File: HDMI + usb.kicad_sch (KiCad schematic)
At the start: 3 parts, among them J2 HDMI_C_1.4, J3 USB_C_Receptacle_USB2.0_16P, J4 USB_C_Receptacle_USB2.0_16P

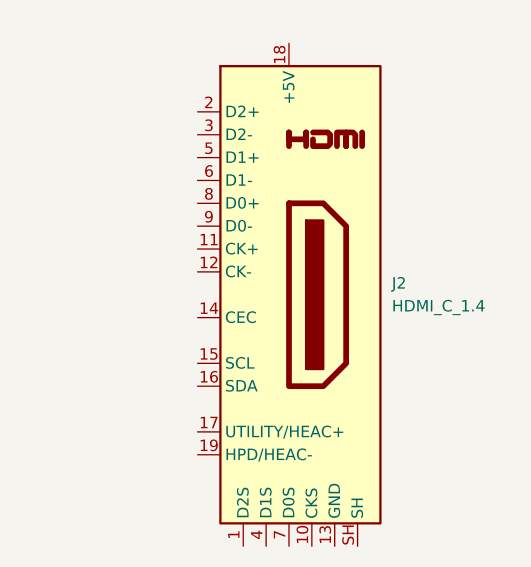
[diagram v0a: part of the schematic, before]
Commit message: расставлены основные блоки и компоненты, подобраны компоненты интерфейса и питания
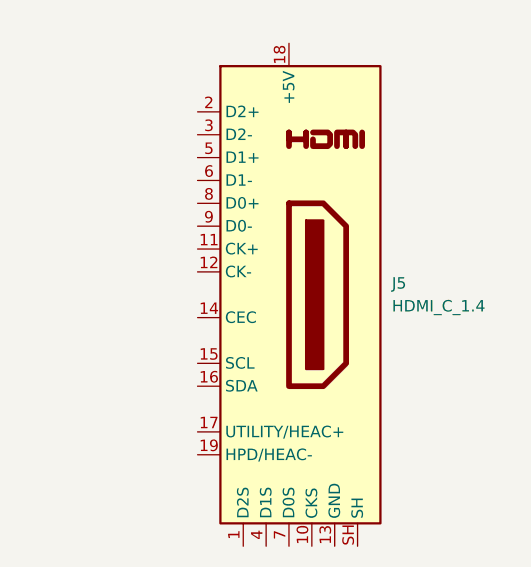
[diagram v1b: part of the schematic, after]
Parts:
- renumbered J2 to J5
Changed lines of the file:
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@@
 		(dnp no)
 		(fields_autoplaced yes)
-		(property "Reference" "J2"
+		(property "Reference" "J5"
 			(at 295.91 147.3199 0)
 			(effects
@@
 			(project ""
 				(path "/b3673bfd-24d8-4789-b63c-c3654dc2bb6e/526c7efe-cb70-49a2-a6ca-c3db3e12ecbe"
-					(reference "J2")
+					(reference "J5")
 					(unit 1)
 				)

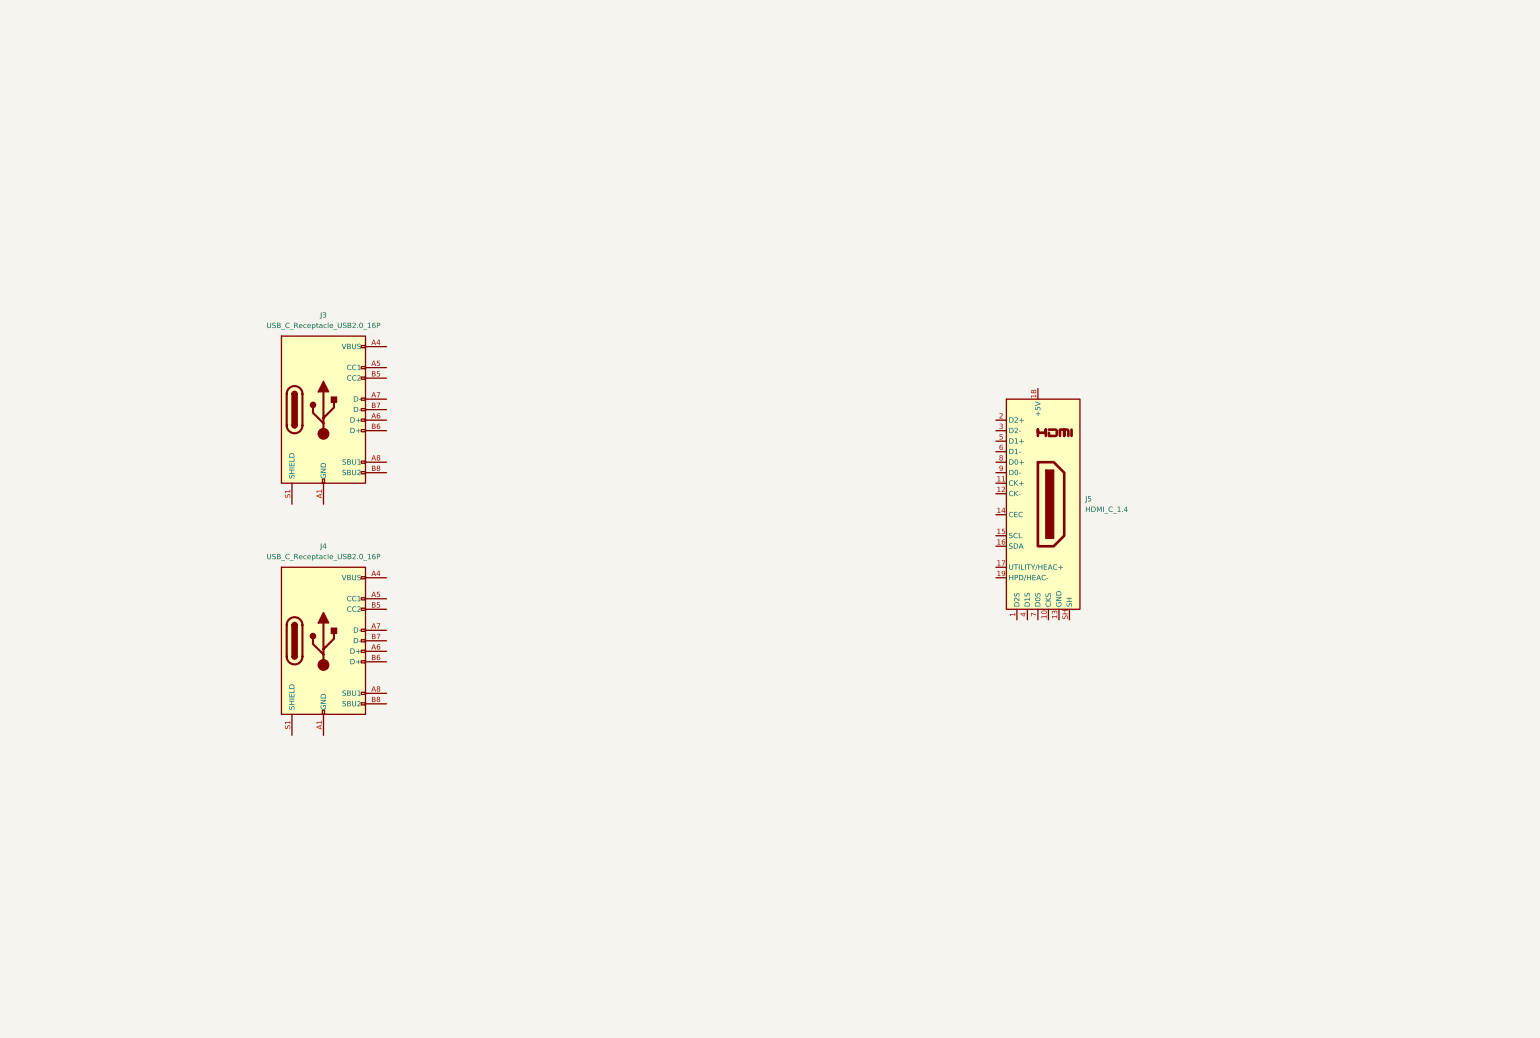
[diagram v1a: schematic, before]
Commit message: Обновлена структура, закончен интерфейс, HDMI Завершено проектирование линий питания и подтяжек для интерфейсов
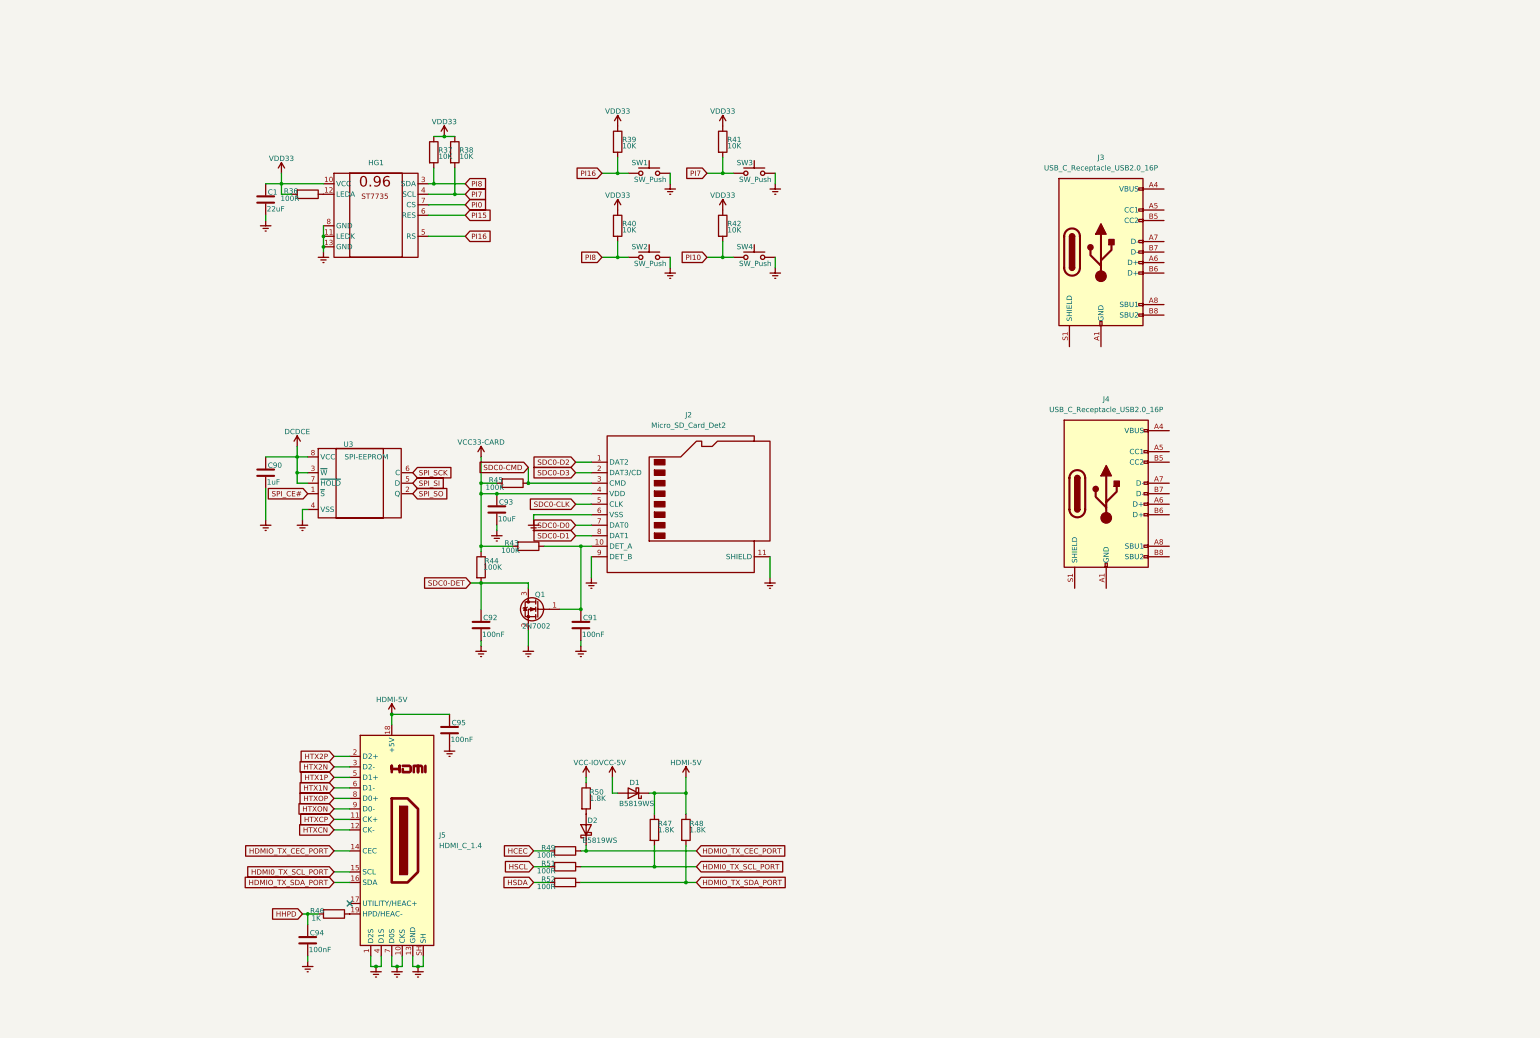
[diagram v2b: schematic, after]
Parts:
- added C1: 22uF, Capacitor_SMD:C_0402_1005Metric, symbol Device:C
- added C90: 1uF, Capacitor_SMD:C_0402_1005Metric, symbol Device:C
- added C91, C92, C94, C95: 100nF, Capacitor_SMD:C_0402_1005Metric, symbol Device:C
- added C93: 10uF, Capacitor_SMD:C_0402_1005Metric, symbol Device:C
- added D1, D2: B5819WS, Diode_SMD:D_SOD-323F, symbol Diode:PMEG4010CEJ
- added HG1: ~, IPS_ST7735_0_96:ST7735 0.96, symbol ST7735 0_96:ST7735_0.96
- added J2: Micro_SD_Card_Det2, Connector_Card:microSD_HC_Hirose_DM3AT-SF-PEJM5, symbol Connector:Micro_SD_Card_Det2
- added Q1: 2N7002, Package_TO_SOT_SMD:SOT-23, symbol Transistor_FET:2N7002
- added R36, R49, R51, R52: 100R, Resistor_SMD:R_0402_1005Metric, symbol Device:R
- added R37, R38, R39, R40, R41, R42: 10K, Resistor_SMD:R_0402_1005Metric, symbol Device:R
- added R43, R44, R45: 100K, Resistor_SMD:R_0402_1005Metric, symbol Device:R
- added R46: 1K, Resistor_SMD:R_0402_1005Metric, symbol Device:R
- added R47, R48, R50: 1.8K, Resistor_SMD:R_0402_1005Metric, symbol Device:R
- added SW1, SW2, SW3, SW4: SW_Push, Button_Switch_SMD:SW_Push_1P1T_NO_Vertical_Wuerth_434133025816, symbol Switch:SW_Push
- added U3: SPI-EEPROM, Package_SO:SOIC-8_3.9x4.9mm_P1.27mm, symbol Memory_EEPROM:M95256-WMN6P
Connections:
- net Earth: now reaches J5.1 (D2S)
- net Earth: now also J5.10 (CKS), J5.13 (GND), J5.4 (D1S), J5.7 (D0S), J5.SH, C1.2, C90.2, C91.2, C92.2, C93.2, C94.2, C95.2, HG1.11 (LEDK), HG1.13 (GND), HG1.8 (GND), J2.11 (SHIELD), J2.6 (VSS), J2.9 (DET_B), Q1.2 (S), SW1.2, SW2.2, SW3.2, SW4.2, U3.4 (VSS)
- net HTXCP: now reaches J5.11 (CK+)
- net HTXCN: now reaches J5.12 (CK-)
- net HDMIO_TX_CEC_PORT: now reaches J5.14 (CEC)
- net HDMIO_TX_CEC_PORT: now also D2.1 (K), R49.1
- net HDMI0_TX_SCL_PORT: now reaches J5.15 (SCL)
- net HDMI0_TX_SCL_PORT: now also R47.2, R51.1
- net HDMIO_TX_SDA_PORT: now reaches J5.16 (SDA)
- net HDMIO_TX_SDA_PORT: now also R48.2, R52.1
- net HDMI-5V: now reaches J5.18 (+5V)
- net HDMI-5V: now also C95.1, D1.1 (K), R47.1, R48.1
- net at J5.19 (HPD/HEAC-): now also R46.1
- net HTX2P: now reaches J5.2 (D2+)
- net HTX2N: now reaches J5.3 (D2-)
- net HTX1P: now reaches J5.5 (D1+)
- net HTX1N: now reaches J5.6 (D1-)
- net HTXOP: now reaches J5.8 (D0+)
- net HTXON: now reaches J5.9 (D0-)
- new net: HG1.12 (LEDA), R36.1
- new net: C91.1, J2.10 (DET_A), Q1.1 (G), R43.1
- new net: D2.2 (A), R50.2
- new net DCDCE: C90.1, U3.3 (~{W}), U3.7 (~{HOLD}), U3.8 (VCC)
- new net HCEC: R49.2
- new net HHPD: C94.1, R46.2
- new net HSCL: R51.2
- new net HSDA: R52.2
- new net PI0: HG1.7 (CS)
- new net PI10: R42.2, SW4.1
- new net PI15: HG1.6 (RES)
- new net PI16: HG1.5 (RS), R39.2, SW1.1
- new net PI7: HG1.4 (SCL), R38.2, R41.2, SW3.1
- new net PI8: HG1.3 (SDA), R37.2, R40.2, SW2.1
- new net SDC0-CLK: J2.5 (CLK)
- new net SDC0-CMD: J2.3 (CMD), R45.1
- new net SDC0-D0: J2.7 (DAT0)
- new net SDC0-D1: J2.8 (DAT1)
- new net SDC0-D2: J2.1 (DAT2)
- new net SDC0-D3: J2.2 (DAT3/CD)
- new net SDC0-DET: C92.1, Q1.3 (D), R44.2
- new net SPI_CE#: U3.1 (~{S})
- new net SPI_SCK: U3.6 (C)
- new net SPI_SI: U3.5 (D)
- new net SPI_SO: U3.2 (Q)
- new net VCC-5V: D1.2 (A)
- new net VCC-IO: R50.1
- new net VCC33-CARD: C93.1, J2.4 (VDD), R43.2, R44.1, R45.2
- new net VDD33: C1.1, HG1.10 (VCC), R36.2, R37.1, R38.1, R39.1, R40.1, R41.1, R42.1
- no-connect marks 0 -> 1
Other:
- moved on the sheet: J3, J4, J5

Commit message: Схема закончена, часть компонентов расставлена на плате
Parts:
- removed J4: USB_C_Receptacle_USB2.0_16P, Connector_USB:USB_C_Receptacle_G-Switch_GT-USB-7010ASV, symbol Connector:USB_C_Receptacle_USB2.0_16P
- added C96, C97: 10uF, Capacitor_SMD:C_0402_1005Metric, symbol Device:C
- added C98: 100nF, Capacitor_SMD:C_0402_1005Metric, symbol Device:C
- added D3, D4: LED-R, LED_SMD:LED_0402_1005Metric, symbol Device:LED
- added D5: AZ5825-01F, ESD:AZ582501F, symbol ESD:AZ5825-01F
- added J5: USB_C_Receptacle_USB2.0_16P, Connector_USB:USB_C_Receptacle_G-Switch_GT-USB-7010ASV, symbol Connector:USB_C_Receptacle_USB2.0_16P
- added R53, R54, R57, R58: 5.1K, Resistor_SMD:R_0402_1005Metric, symbol Device:R
- added R55, R56: 36K, Resistor_SMD:R_0402_1005Metric, symbol Device:R
- renumbered C94 to C89, C1 to C90, C90 to C91, C95 to C92, C92 to C93, C93 to C94, C91 to C95, D2 to D1, D1 to D2, J5 to J2, J2 to J3, J3 to J4, R46 to R36, R36 to R37, R37 to R38, R38 to R39, R49 to R40, R51 to R41, R52 to R42, R44 to R43, R50 to R44, R43 to R46, R39 to R49, R40 to R50, R41 to R51, R42 to R52
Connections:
- net Earth: now also J4.A1 (GND), J4.A12 (GND), J4.B1 (GND), J4.B12 (GND), J4.S1 (SHIELD), C96.2, C97.2, C98.2, D3.1 (K), D4.1 (K), D5.2, J5.A1 (GND), J5.A12 (GND), J5.B1 (GND), J5.B12 (GND), J5.S1 (SHIELD), R55.2, R56.2, R57.2, R58.2
- net PI16: no longer R49.2, SW1.1
- net PI7: no longer HG1.4 (SCL), R39.2
- net PI8: no longer HG1.3 (SDA), R38.2
- net VCC-5V: now also J4.A4 (VBUS), J4.A9 (VBUS), J4.B4 (VBUS), J4.B9 (VBUS), C96.1, C97.1, C98.1, D5.1, J5.A4 (VBUS), J5.A9 (VBUS), J5.B4 (VBUS), J5.B9 (VBUS)
- net VDD33: now also R53.1
- net at J4.A5 (CC1): now also R55.1
- net USB0-DP: now reaches J4.A6 (D+)
- net USB0-DP: now also J4.B6 (D+)
- net USB0-DM: now reaches J4.A7 (D-)
- net USB0-DM: now also J4.B7 (D-)
- net at J4.B5 (CC2): now also R56.1
- new net: J5.A5 (CC1), R57.1
- new net: J5.B5 (CC2), R58.1
- new net: D4.2 (A), R54.2
- new net: D3.2 (A), R53.2
- new net PI12: R49.2, SW1.1
- new net SPI1_CLK: HG1.4 (SCL), R39.2
- new net SPI1_MOSI: HG1.3 (SDA), R38.2
- new net STATUS-:ED: R54.1
- new net USB1-DM: J5.A7 (D-), J5.B7 (D-)
- new net USB1-DP: J5.A6 (D+), J5.B6 (D+)
- no-connect marks 1 -> 5
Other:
- note added: "HDMI"
- note added: "INTERFACE"
- note added: "LED"
- note added: "MEMORY"
- note added: "USB0"
- note added: "USB1"
- moved on the sheet: C89, C90, C91, C92, C93, C94, C95, D1, D2, HG1, J2, J3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

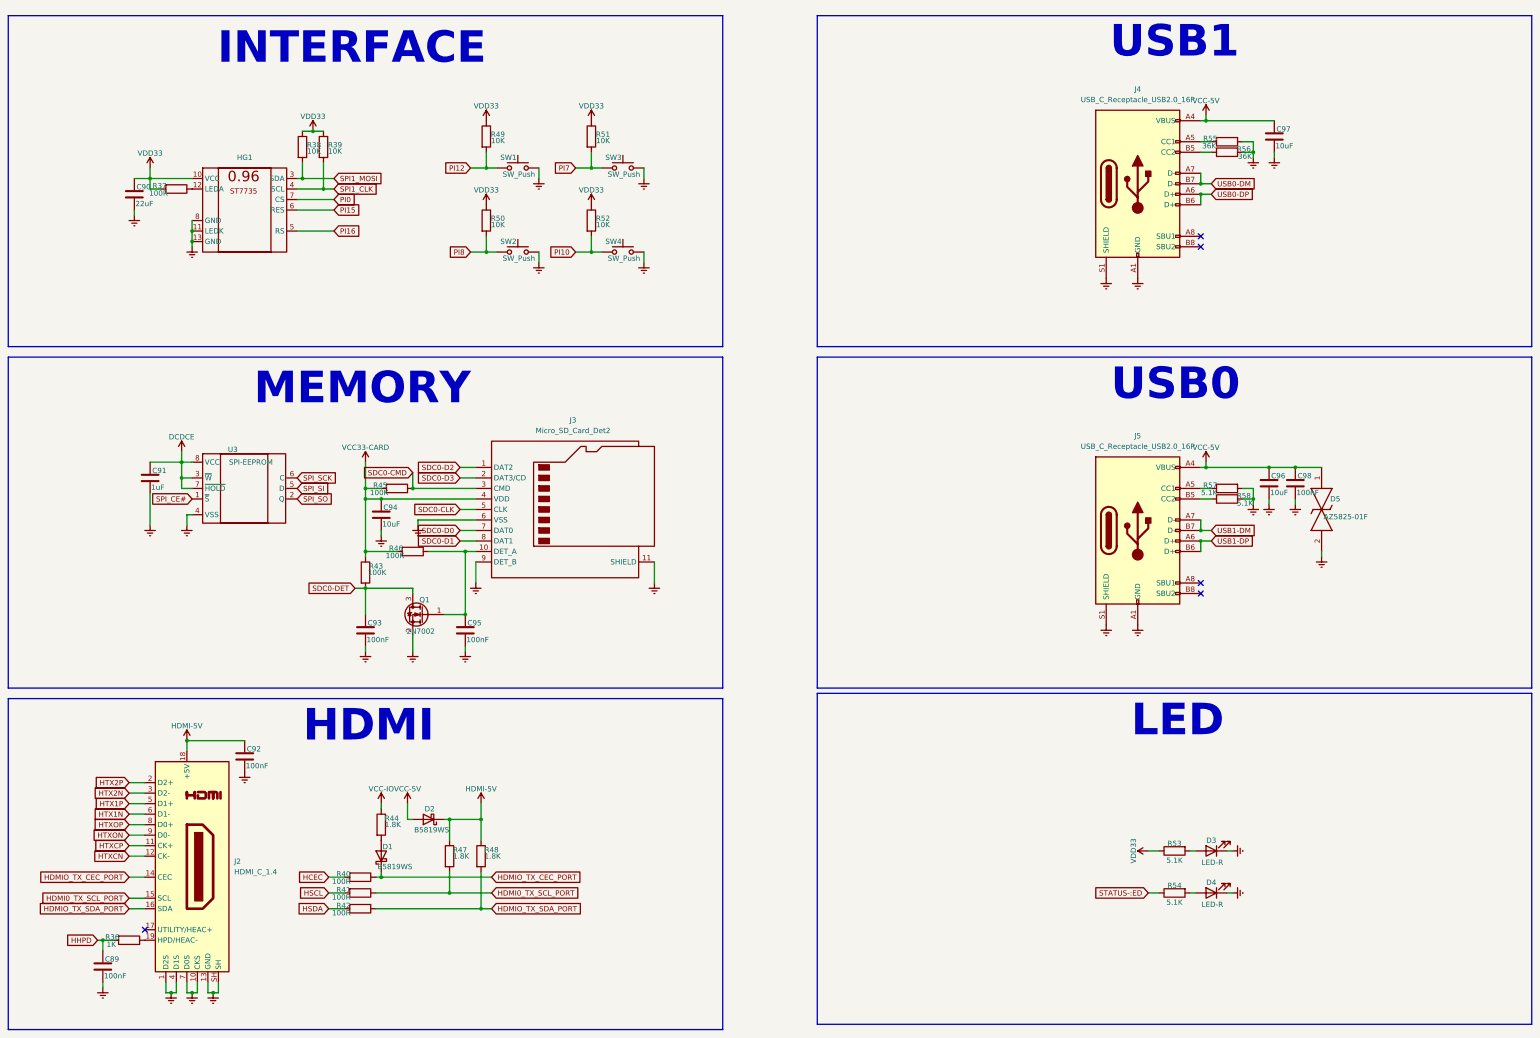
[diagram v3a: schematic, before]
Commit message: Кучка исправлений, переместил SD карту, дисплей, в целом компоновка чуть другая Небольшие исправления в схеме 🤠
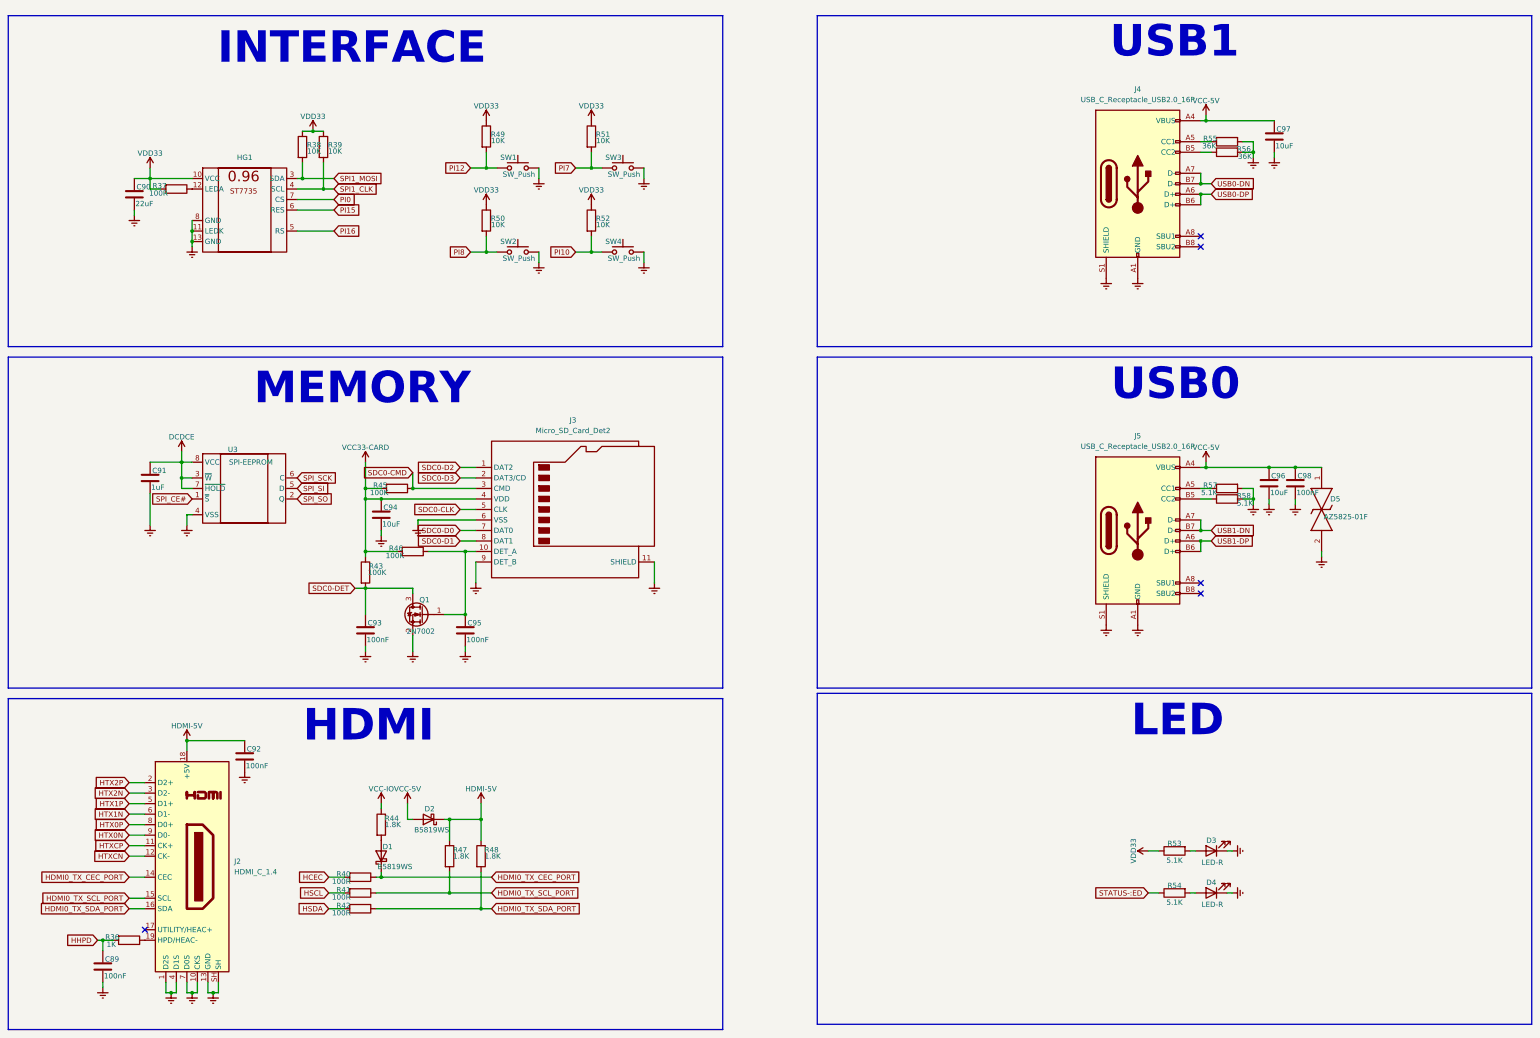
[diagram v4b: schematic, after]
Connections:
- net HDMIO_TX_CEC_PORT renamed HDMI0_TX_CEC_PORT
- net HDMIO_TX_SDA_PORT renamed HDMI0_TX_SDA_PORT
- net HTXON renamed HTX0N
- net HTXOP renamed HTX0P
- net USB0-DM renamed USB0-DN
- net USB1-DM renamed USB1-DN

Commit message: Проведены все линии данных, осталось лишь сделать полигонами питание и шелкографию исправить :)
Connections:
- net STATUS-:ED renamed STATUS-LED
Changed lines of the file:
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@@
 		)
 	)
-	(global_label "STATUS-:ED"
+	(global_label "STATUS-LED"
 		(shape input)
 		(at 311.15 242.57 180)
@@
 		)
 		(property "Intersheetrefs" "${INTERSHEET_REFS}"
-			(at 301.5358 242.57 0)
+			(at 301.1834 242.57 0)
 			(effects
 				(font
@@
 			)
 		)
+	)
+	(netclass_flag ""
+		(length 2.54)
+		(shape round)
+		(at 334.01 55.88 0)
+		(fields_autoplaced yes)
+		(effects
+			(font
+				(size 1.27 1.27)
+			)
+			(justify left bottom)
+		)
+		(property "Netclass" "Power"
+			(at 334.7085 53.34 0)
+			(effects
+				(font
+					(size 1.27 1.27)
+				)
+				(justify left)
+			)
+		)
+		(property "Component Class" ""
+			(at 299.72 -121.92 0)
+			(effects
+				(font
+					(size 1.27 1.27)
+					(italic yes)
+				)
+			)
+		)
+	)
+	(netclass_flag ""
+		(length 2.54)
+		(shape round)
+		(at 332.74 139.7 0)
+		(fields_autoplaced yes)
+		(effects
+			(font
+				(size 1.27 1.27)
+			)
+			(justify left bottom)
+		)
+		(property "Netclass" "Power"
+			(at 333.4385 137.16 0)
+			(effects
+				(font
+					(size 1.27 1.27)
+				)
+				(justify left)
+			)
+		)
+		(property "Component Class" ""
+			(at 298.45 -38.1 0)
+			(effects
+				(font
+					(size 1.27 1.27)
+					(italic yes)
+				)
+			)
+		)

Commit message: Исправление УГО по ГОСТу, добавление 3D моделей
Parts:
- U3: value SPI-EEPROM -> M24M02-DRMN6TP
- renumbered C90 to C88, C91 to C89, C89 to C90, C92 to C91, C93 to C92, C94 to C93, C95 to C94, C98 to C95, C97 to C96, C96 to C97, D5 to D3, D3 to D4, D4 to D5, R37 to R34, R36 to R35, R38 to R36, R39 to R37, R43 to R38, R40 to R39, R41 to R40, R42 to R41, R45 to R42, R46 to R43, R49 to R45, R50 to R46, R51 to R49, R52 to R50, R55 to R51, R56 to R52, R57 to R53, R58 to R54, R53 to R55, R54 to R56, J2 to X2, J3 to X3, J4 to X4, J5 to X5
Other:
- company: @madjogger -> РТУ МИРЭА
- moved on the sheet: C90, C91, C92, C93, C94, C95, C96, C97, D1, D2, D3, Q1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
